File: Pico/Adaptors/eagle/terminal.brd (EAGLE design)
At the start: 60 x 41.3 mm, 11 parts, among them J1 SCREW-TERMINAL-3P-3470080P1, J10 SCREW-TERMINAL-2P-3470110P1, J2 SCREW-TERMINAL-3P-3470080P1, J3 SCREW-TERMINAL-3P-3470080P1, J4 SCREW-TERMINAL-2P-3470110P1, J5 SCREW-TERMINAL-3P-3470080P1, J6 SCREW-TERMINAL-3P-3470080P1, J7 SCREW-TERMINAL-3P-3470080P1, J8 SCREW-TERMINAL-3P-3470080P1, J9 SCREW-TERMINAL-2P-3470110P1

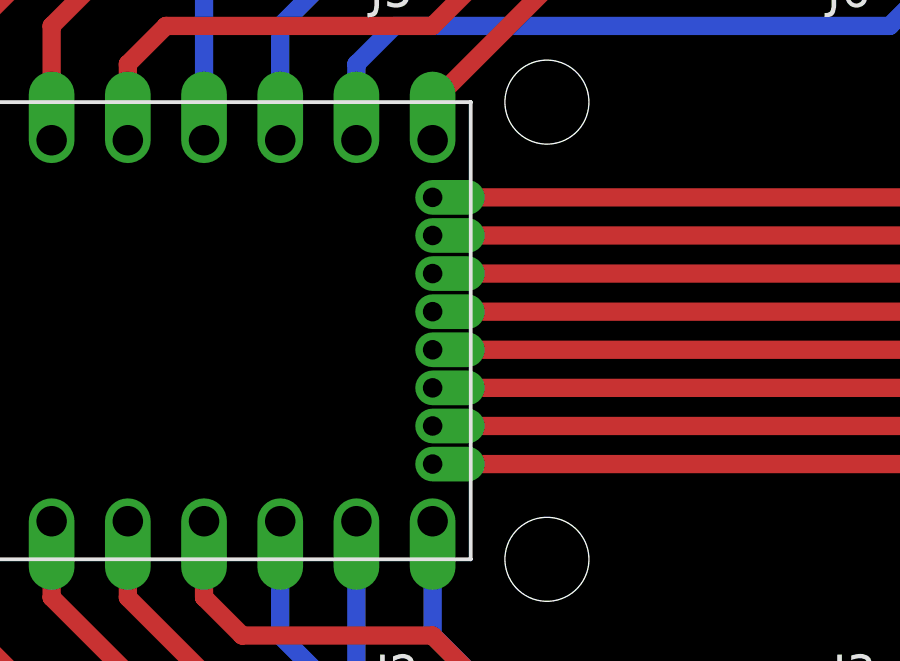
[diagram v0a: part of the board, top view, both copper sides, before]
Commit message: nrf24 adaptor, and DRC
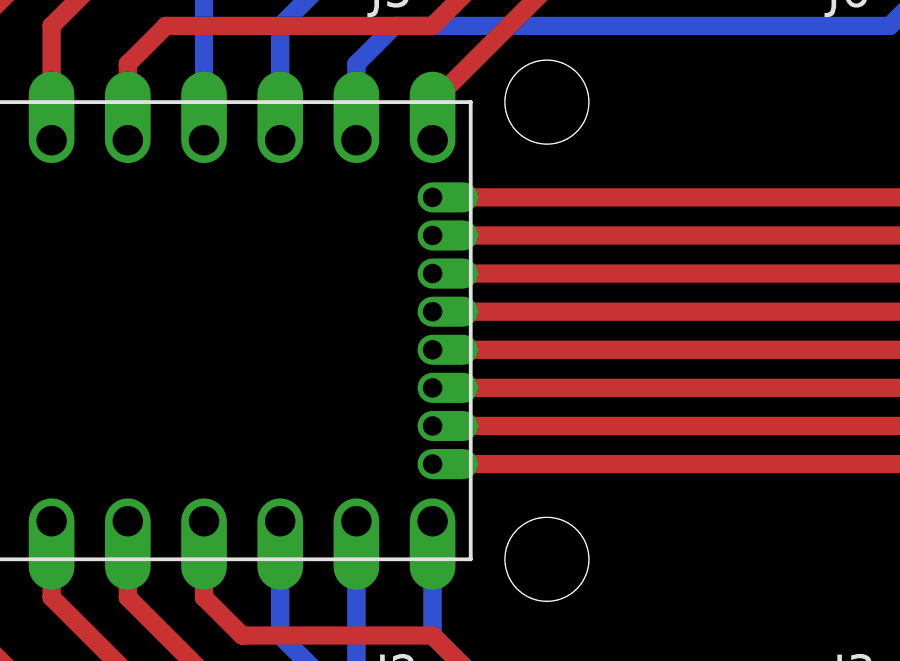
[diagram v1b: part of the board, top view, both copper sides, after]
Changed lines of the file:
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@@
 </class>
 </classes>
-<designrules name="default">
+<designrules name="oshpark-2layer">
 <description language="de">&lt;b&gt;EAGLE Design Rules&lt;/b&gt;
 &lt;p&gt;
@@
 Einstellungen hier und speichern die Design Rules unter
 einem neuen Namen ab.</description>
-<description language="en">&lt;b&gt;EAGLE Design Rules&lt;/b&gt;
+<description language="en">&lt;b&gt;Laen's PCB Order Design Rules&lt;/b&gt;
 &lt;p&gt;
-The default Design Rules have been set to cover
-a wide range of applications. Your particular design
-may have different requirements, so please make the
-necessary adjustments and save your customized
-design rules under a new name.</description>
+Please make sure your boards conform to these design rules.</description>
 <param name="layerSetup" value="(1*16)"/>
-<param name="mtCopper" value="0.035mm 0.035mm 0.035mm 0.035mm 0.035mm 0.035mm 0.035mm 0.035mm 0.035mm 0.035mm 0.035mm 0.035mm 0.035mm 0.035mm 0.035mm 0.035mm"/>
-<param name="mtIsolate" value="1.5mm 0.15mm 0.2mm 0.15mm 0.2mm 0.15mm 0.2mm 0.15mm 0.2mm 0.15mm 0.2mm 0.15mm 0.2mm 0.15mm 0.2mm"/>
-<param name="mdWireWire" value="8mil"/>
-<param name="mdWirePad" value="8mil"/>
-<param name="mdWireVia" value="8mil"/>
-<param name="mdPadPad" value="8mil"/>
-<param name="mdPadVia" value="8mil"/>
-<param name="mdViaVia" value="8mil"/>
-<param name="mdSmdPad" value="8mil"/>
-<param name="mdSmdVia" value="8mil"/>
-<param name="mdSmdSmd" value="8mil"/>
+<param name="mtCopper" value="0.0356mm 0.0356mm 0.0356mm 0.0356mm 0.0356mm 0.0356mm 0.0356mm 0.0356mm 0.0356mm 0.0356mm 0.0356mm 0.0356mm 0.0356mm 0.0356mm 0.0356mm 0.0356mm"/>
+<param name="mtIsolate" value="1.5011mm 0.1499mm 0.2007mm 0.1499mm 0.2007mm 0.1499mm 0.2007mm 0.1499mm 0.2007mm 0.1499mm 0.2007mm 0.1499mm 0.2007mm 0.1499mm 0.2007mm"/>
+<param name="mdWireWire" value="6mil"/>
+<param name="mdWirePad" value="6mil"/>
+<param name="mdWireVia" value="6mil"/>
+<param name="mdPadPad" value="6mil"/>
+<param name="mdPadVia" value="6mil"/>
+<param name="mdViaVia" value="6mil"/>
+<param name="mdSmdPad" value="6mil"/>
+<param name="mdSmdVia" value="6mil"/>
+<param name="mdSmdSmd" value="6mil"/>
 <param name="mdViaViaSameLayer" value="8mil"/>
 <param name="mnLayersViaInSmd" value="2"/>
-<param name="mdCopperDimension" value="40mil"/>
-<param name="mdDrill" value="8mil"/>
+<param name="mdCopperDimension" value="15mil"/>
+<param name="mdDrill" value="6mil"/>
 <param name="mdSmdStop" value="0mil"/>
-<param name="msWidth" value="10mil"/>
-<param name="msDrill" value="24mil"/>
-<param name="msMicroVia" value="9.99mm"/>
+<param name="msWidth" value="6mil"/>
+<param name="msDrill" value="13mil"/>
+<param name="msMicroVia" value="13mil"/>
 <param name="msBlindViaRatio" value="0.5"/>
 <param name="rvPadTop" value="0.25"/>
@@
 <param name="rvMicroViaOuter" value="0.25"/>
 <param name="rvMicroViaInner" value="0.25"/>
-<param name="rlMinPadTop" value="10mil"/>
+<param name="rlMinPadTop" value="7mil"/>
 <param name="rlMaxPadTop" value="20mil"/>
-<param name="rlMinPadInner" value="10mil"/>
+<param name="rlMinPadInner" value="7mil"/>
 <param name="rlMaxPadInner" value="20mil"/>
-<param name="rlMinPadBottom" value="10mil"/>
+<param name="rlMinPadBottom" value="7mil"/>
 <param name="rlMaxPadBottom" value="20mil"/>
-<param name="rlMinViaOuter" value="8mil"/>
+<param name="rlMinViaOuter" value="7mil"/>
 <param name="rlMaxViaOuter" value="20mil"/>
-<param name="rlMinViaInner" value="8mil"/>
+<param name="rlMinViaInner" value="7mil"/>
 <param name="rlMaxViaInner" value="20mil"/>
 <param name="rlMinMicroViaOuter" value="4mil"/>

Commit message: tweaking
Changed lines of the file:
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@@
 </class>
 </classes>
-<designrules name="oshpark-2layer">
+<designrules name="oshpark">
 <description language="de">&lt;b&gt;EAGLE Design Rules&lt;/b&gt;
 &lt;p&gt;
@@
 <param name="mtCopper" value="0.0356mm 0.0356mm 0.0356mm 0.0356mm 0.0356mm 0.0356mm 0.0356mm 0.0356mm 0.0356mm 0.0356mm 0.0356mm 0.0356mm 0.0356mm 0.0356mm 0.0356mm 0.0356mm"/>
 <param name="mtIsolate" value="1.5011mm 0.1499mm 0.2007mm 0.1499mm 0.2007mm 0.1499mm 0.2007mm 0.1499mm 0.2007mm 0.1499mm 0.2007mm 0.1499mm 0.2007mm 0.1499mm 0.2007mm"/>
-<param name="mdWireWire" value="6mil"/>
+<param name="mdWireWire" value="8mil"/>
 <param name="mdWirePad" value="6mil"/>
 <param name="mdWireVia" value="6mil"/>
@@
 <param name="mdDrill" value="6mil"/>
 <param name="mdSmdStop" value="0mil"/>
-<param name="msWidth" value="6mil"/>
+<param name="msWidth" value="10mil"/>
 <param name="msDrill" value="13mil"/>
 <param name="msMicroVia" value="13mil"/>
@@
 <param name="mlMinCreamFrame" value="0mil"/>
 <param name="mlMaxCreamFrame" value="0mil"/>
-<param name="mlViaStopLimit" value="0mil"/>
+<param name="mlViaStopLimit" value="15mil"/>
 <param name="srRoundness" value="0"/>
 <param name="srMinRoundness" value="0mil"/>
@@
 <element name="J8" library="OPL Eagle Library" package="3P-5.0" value="SCREW-TERMINAL-3P-3470080P1" x="55.88" y="17.78" rot="R90"/>
 <element name="J9" library="OPL Eagle Library" package="2P-5.0" value="SCREW-TERMINAL-2P-3470110P1" x="55.88" y="5.08" rot="R90"/>
-<element name="J4" library="OPL Eagle Library" package="2P-5.0" value="SCREW-TERMINAL-2P-3470110P1" x="5.08" y="36.83"/>
+<element name="J4" library="OPL Eagle Library" package="2P-5.0" value="SCREW-TERMINAL-2P-3470110P1" x="5.08" y="36.83" smashed="yes">
+<attribute name="NAME" x="5.08" y="31.115" size="1.27" layer="25" ratio="12"/>
+<attribute name="VALUE" x="2.54" y="36.83" size="0.635" layer="27" ratio="10"/>
+</element>
 <element name="J10" library="OPL Eagle Library" package="2P-5.0" value="SCREW-TERMINAL-2P-3470110P1" x="45.72" y="36.83" rot="R180"/>
 </elements>
